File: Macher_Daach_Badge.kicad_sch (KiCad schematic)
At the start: 14 parts, among them IC1 ATMEGA328P-P, P1 CONN_01X01, P2 SUPPLY, P3 ISP, P4 UART, SW1 Button 1, SW2 Button 2, SW3 Power Switch

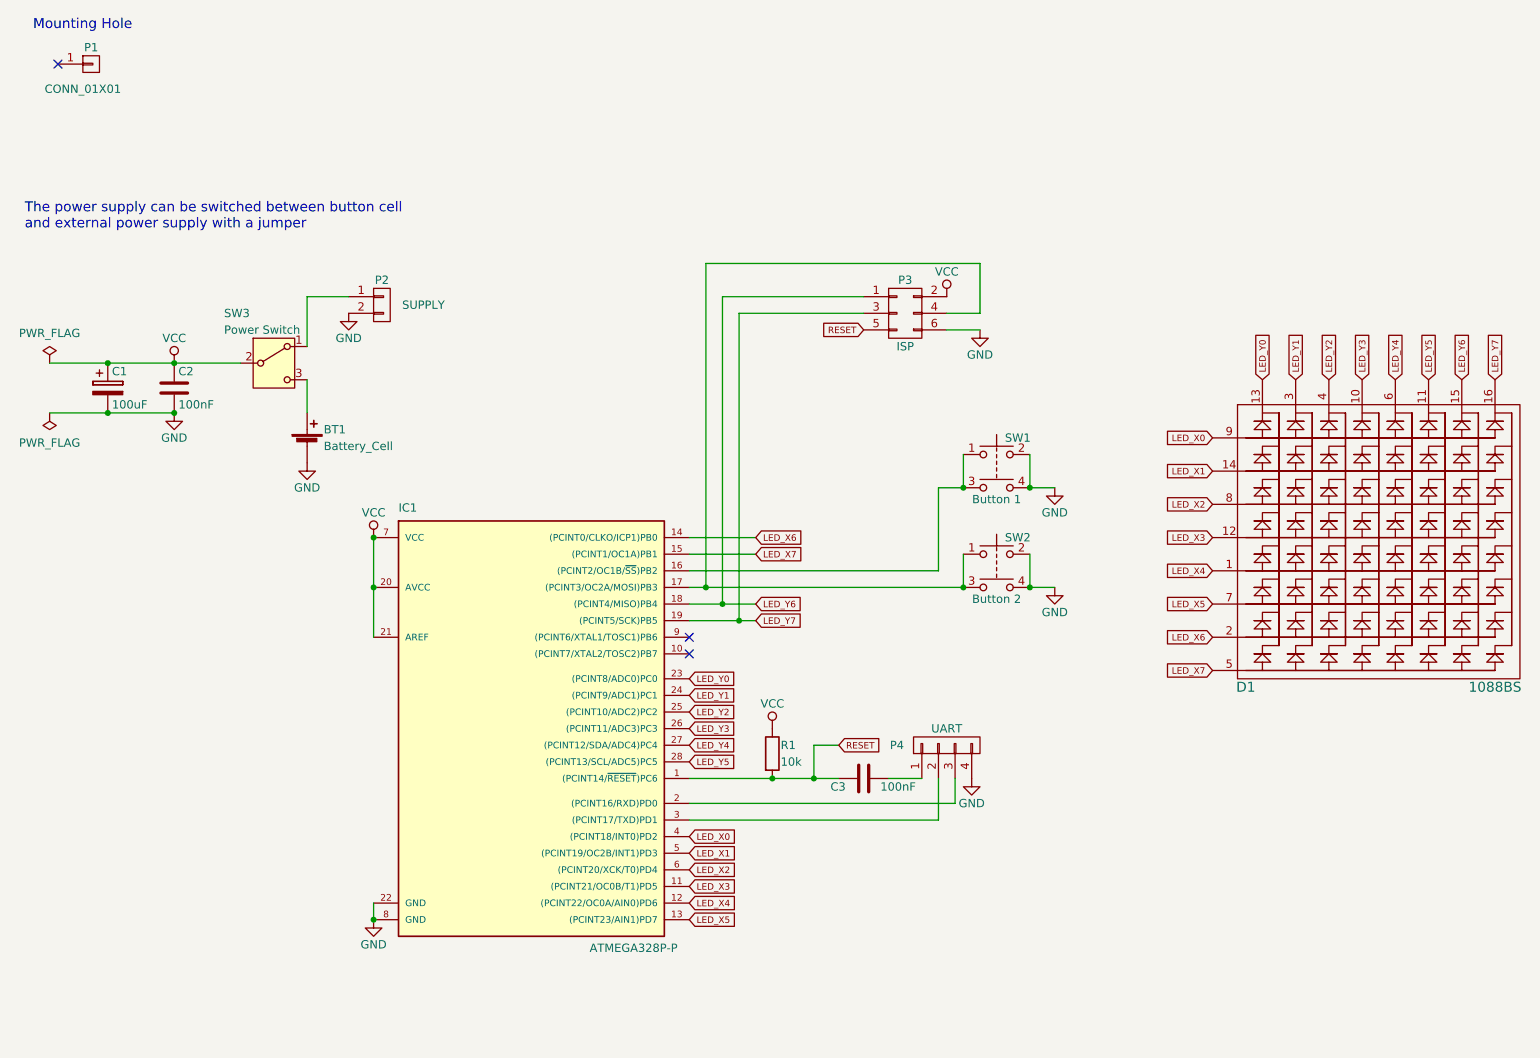
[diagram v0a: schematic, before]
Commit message: first changes for v4.0 with buzzer
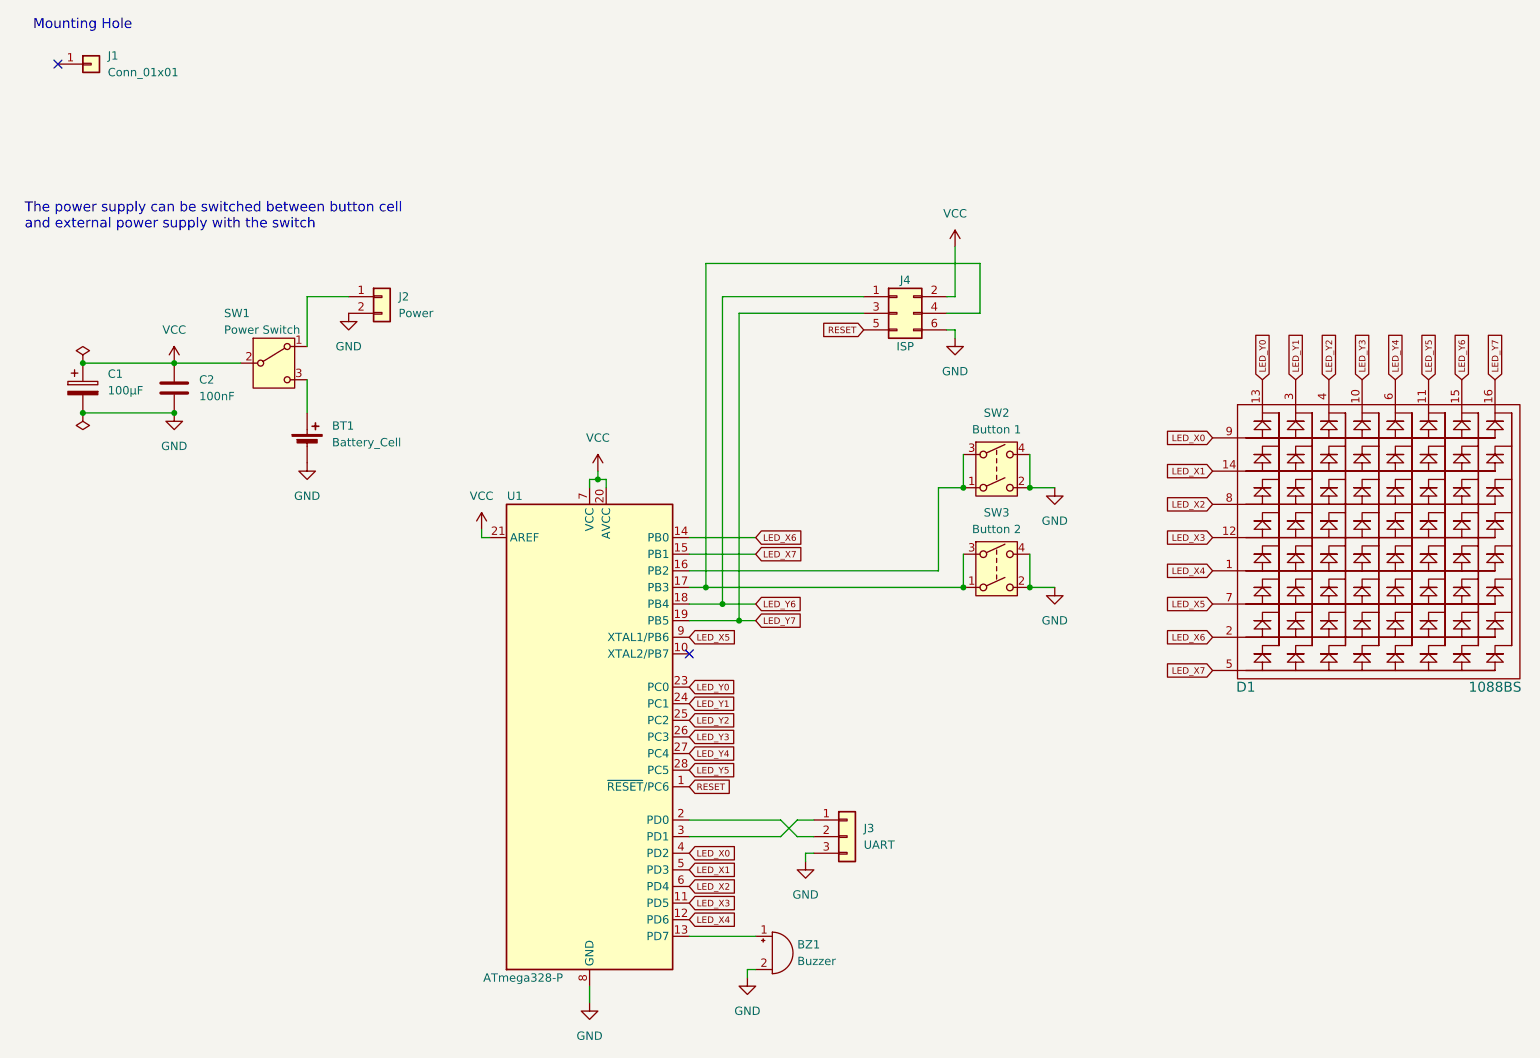
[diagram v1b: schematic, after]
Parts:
- removed BT1: Battery_Cell, 1088BS:Knopfzellenclip_20mm, symbol Macher_Daach_Badge-rescue:Battery_Cell
- removed C1: 100uF, Capacitors_ThroughHole:C_Radial_D5_L6_P2.5, symbol Macher_Daach_Badge-rescue:CP
- removed C2, C3: 100nF, Capacitors_ThroughHole:C_Disc_D3_P2.5, symbol Macher_Daach_Badge-rescue:C
- removed IC1: ATMEGA328P-P, Housings_DIP:DIP-28_W7.62mm_LongPads, symbol Macher_Daach_Badge-rescue:ATMEGA328P-P
- removed P1: CONN_01X01, Mounting_Holes:MountingHole_5.3mm_M5_DIN965_Pad, symbol Macher_Daach_Badge-rescue:CONN_01X01
- removed P2: SUPPLY, Pin_Headers:Pin_Header_Straight_1x02, symbol Macher_Daach_Badge-rescue:CONN_01X02
- removed P3: ISP, Pin_Headers:Pin_Header_Straight_2x03, symbol Macher_Daach_Badge-rescue:CONN_02X03
- removed P4: UART, Pin_Headers:Pin_Header_Straight_1x04, symbol Macher_Daach_Badge-rescue:CONN_01X04
- removed R1: 10k, Resistors_ThroughHole:Resistor_Horizontal_RM7mm, symbol Macher_Daach_Badge-rescue:R
- removed SW1: Button 1, Kurzhubtaster:Kurzhubtaster, symbol Macher_Daach_Badge-rescue:SW_Push_Dual
- removed SW2: Button 2, Kurzhubtaster:Kurzhubtaster, symbol Macher_Daach_Badge-rescue:SW_Push_Dual
- added BT1: Battery_Cell, 1088BS:Knopfzellenclip_20mm, symbol Device:Battery_Cell
- added BZ1: Buzzer, HC9042:Buzzer_9x4.2RM4, symbol Device:Buzzer
- added C1: 100µF, Capacitor_THT:CP_Radial_D5.0mm_P2.50mm, symbol Device:C_Polarized
- added C2: 100nF, Capacitor_THT:C_Disc_D3.4mm_W2.1mm_P2.50mm, symbol Device:C
- added J1: Conn_01x01, MountingHole:MountingHole_5.3mm_M5_DIN965_Pad, symbol Connector_Generic:Conn_01x01
- added J2: Power, Connector_PinHeader_2.54mm:PinHeader_1x02_P2.54mm_Vertical, symbol Connector_Generic:Conn_01x02
- added J3: UART, Connector_PinHeader_2.54mm:PinHeader_1x03_P2.54mm_Vertical, symbol Connector_Generic:Conn_01x03
- added J4: ISP, Connector_PinHeader_2.54mm:PinHeader_2x03_P2.54mm_Vertical, symbol Connector_Generic:Conn_02x03_Odd_Even
- added SW2: Button 1, Kurzhubtaster:Kurzhubtaster, symbol Switch:SW_DPST
- added SW3: Button 2, Kurzhubtaster:Kurzhubtaster, symbol Switch:SW_DPST
- added U1: ATmega328-P, Package_DIP:DIP-28_W7.62mm, symbol MCU_Microchip_ATmega:ATmega328-P
- renumbered SW3 to SW1
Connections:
- net GND: now also BT1.2 (-), BZ1.2 (-), C1.2, C2.2, J2.2 (Pin_2), J3.3 (Pin_3), J4.6 (Pin_6), SW2.2, SW2.4, SW3.2, SW3.4, U1.22 (GND), U1.8 (GND)
- net LED_X0: now also U1.4 (PD2)
- net LED_X1: now also U1.5 (PD3)
- net LED_X2: now also U1.6 (PD4)
- net LED_X3: now also U1.11 (PD5)
- net LED_X4: now also U1.12 (PD6)
- net LED_X5: now also U1.9 (XTAL1/PB6)
- net LED_X6: now also U1.14 (PB0)
- net LED_X7: now also U1.15 (PB1)
- net LED_Y0: now also U1.23 (PC0)
- net LED_Y1: now also U1.24 (PC1)
- net LED_Y2: now also U1.25 (PC2)
- net LED_Y3: now also U1.26 (PC3)
- net LED_Y4: now also U1.27 (PC4)
- net LED_Y5: now also U1.28 (PC5)
- net LED_Y6: now also J4.1 (Pin_1), U1.18 (PB4)
- net LED_Y7: now also J4.3 (Pin_3), U1.19 (PB5)
- net RESET: now also J4.5 (Pin_5), U1.1 (~{RESET}/PC6)
- net VCC: now also C1.1, C2.1, J4.2 (Pin_2), U1.20 (AVCC), U1.21 (AREF), U1.7 (VCC)
- net at SW1.3 (C): now also BT1.1 (+)
- net at SW1.1 (A): now also J2.1 (Pin_1)
- new net: J3.1 (Pin_1), U1.3 (PD1)
- new net: J3.2 (Pin_2), U1.2 (PD0)
- new net: J4.4 (Pin_4), SW3.1, SW3.3, U1.17 (PB3)
- new net: SW2.1, SW2.3, U1.16 (PB2)
- new net: BZ1.1 (+), U1.13 (PD7)
- no-connect marks 3 -> 2
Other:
- note added: "The power supply can be switched between button cell and external power supply with the switch"
- note removed: "The power supply can be switched between button cell and external power supply with a jumper"
- title: Macher Daach Badge -> Macherdaach Badge

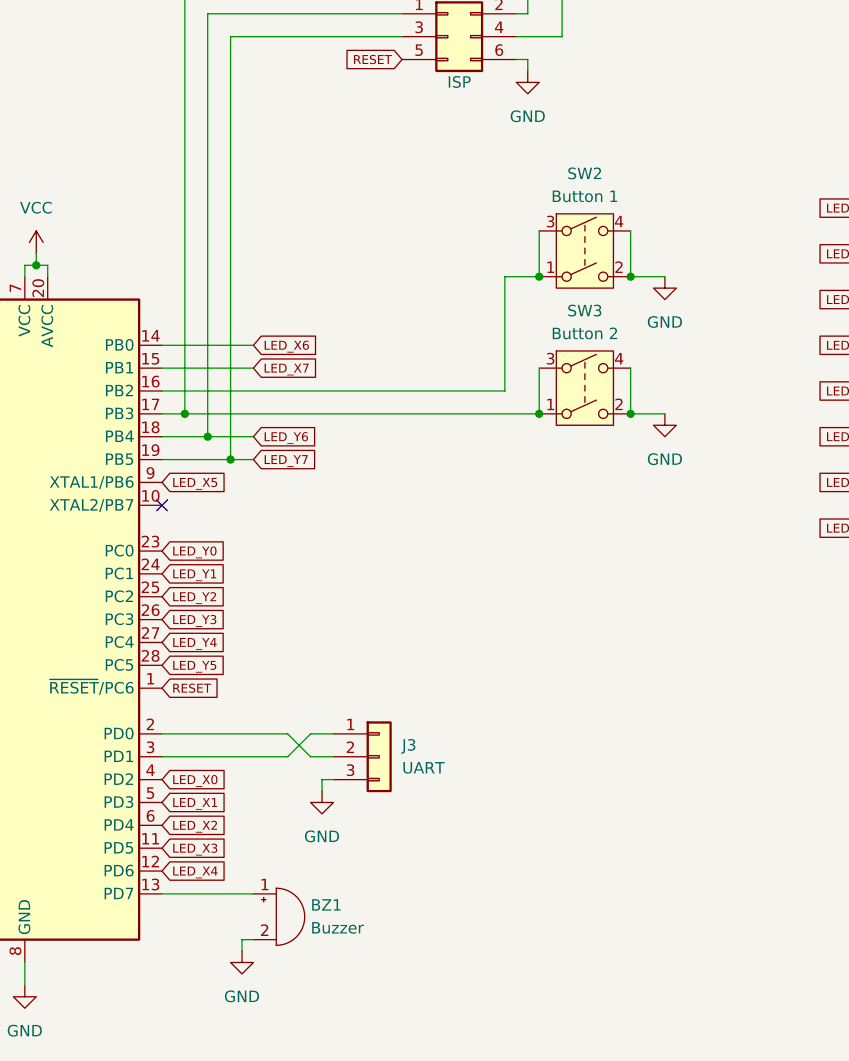
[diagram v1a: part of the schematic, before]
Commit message: move buzzer pin from PD7 to PB1
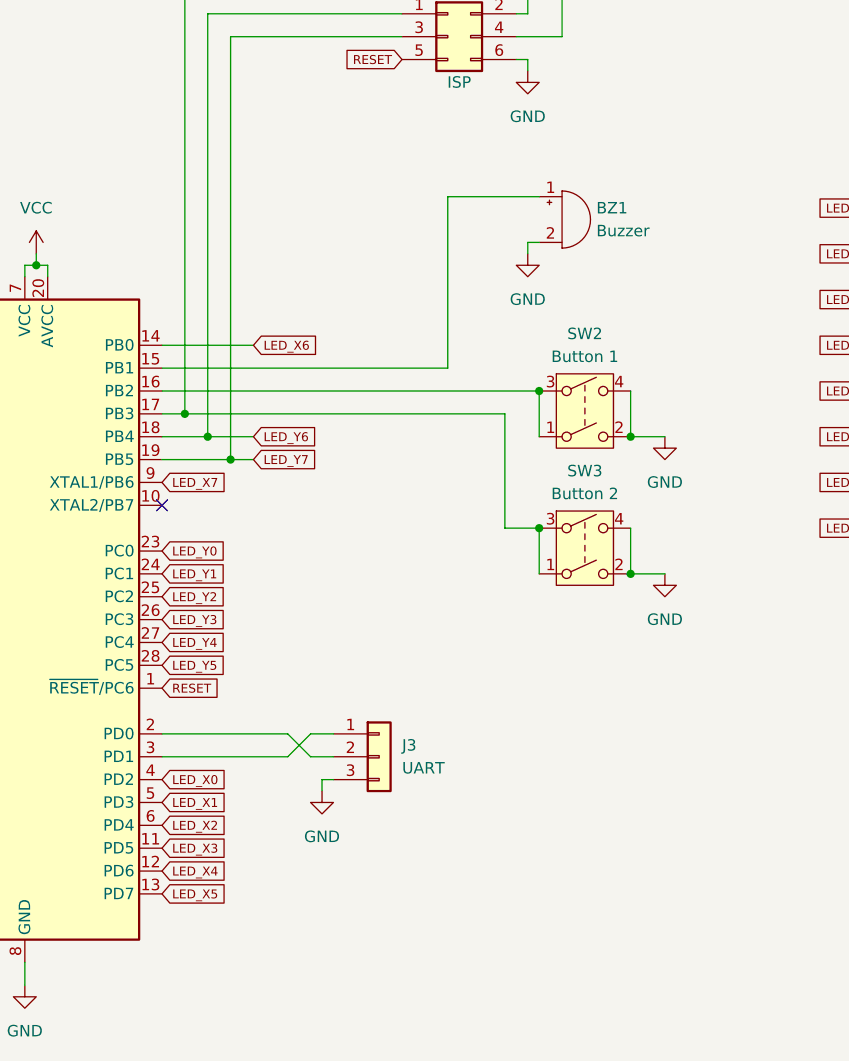
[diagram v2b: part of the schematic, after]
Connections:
- net LED_X5: now also U1.13 (PD7); no longer U1.9 (XTAL1/PB6)
- net LED_X7: now also U1.9 (XTAL1/PB6); no longer U1.15 (PB1)
- net at BZ1.1 (+): now also U1.15 (PB1); no longer U1.13 (PD7)
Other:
- moved on the sheet: BZ1, SW2, SW3
